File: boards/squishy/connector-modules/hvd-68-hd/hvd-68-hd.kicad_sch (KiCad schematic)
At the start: 14 parts, among them J1 SCSI PHY Mezz, J3 Conn_01x04, J4 HD-68, U1 M24C02-RMC

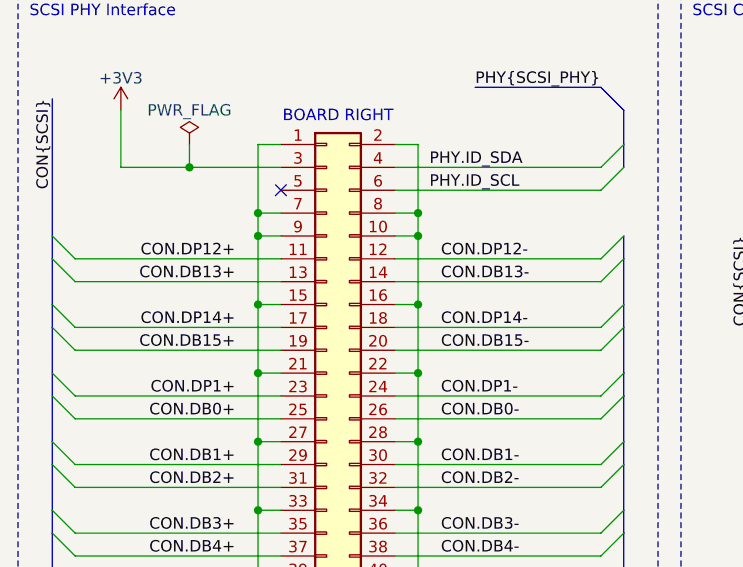
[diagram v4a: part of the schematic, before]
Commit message: squishy: connectors: s/DP12/DB12/g s/DP14/DB14/g
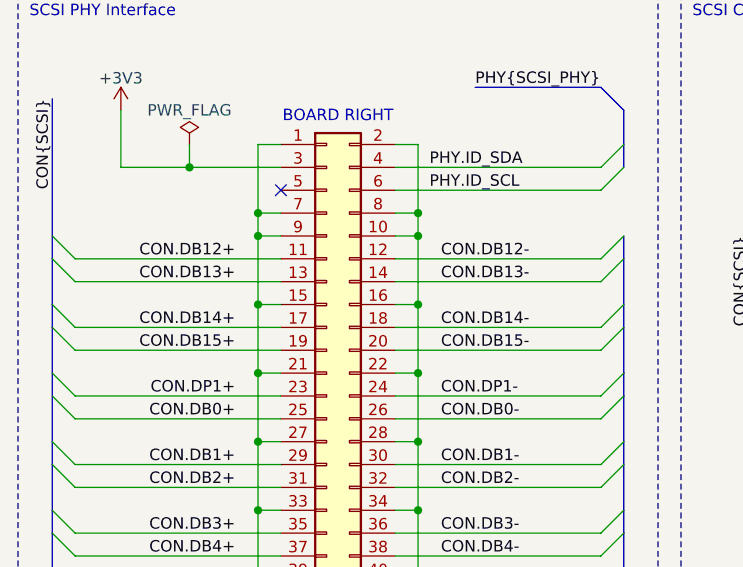
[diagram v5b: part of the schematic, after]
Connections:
- net CON.DP12+ is gone; now on net CON.DB12+: J1.11 (Pin_11)
- net CON.DP12- is gone; now on net CON.DB12-: J1.12 (Pin_12)
- net CON.DP14+ is gone; now on net CON.DB14+: J1.17 (Pin_17)
- net CON.DP14- is gone; now on net CON.DB14-: J1.18 (Pin_18)
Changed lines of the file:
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@@
 		)
 	)
-	(label "CON.DP14-"
+	(label "CON.DB14-"
 		(at 60.96 52.07 0)
 		(fields_autoplaced yes)
@@
 		)
 	)
-	(label "CON.DP12+"
+	(label "CON.DB12+"
 		(at 38.1 44.45 180)
 		(fields_autoplaced yes)
@@
 		)
 	)
-	(label "CON.DP12-"
+	(label "CON.DB12-"
 		(at 60.96 44.45 0)
 		(fields_autoplaced yes)
@@
 		)
 	)
-	(label "CON.DP14+"
+	(label "CON.DB14+"
 		(at 38.1 52.07 180)
 		(fields_autoplaced yes)

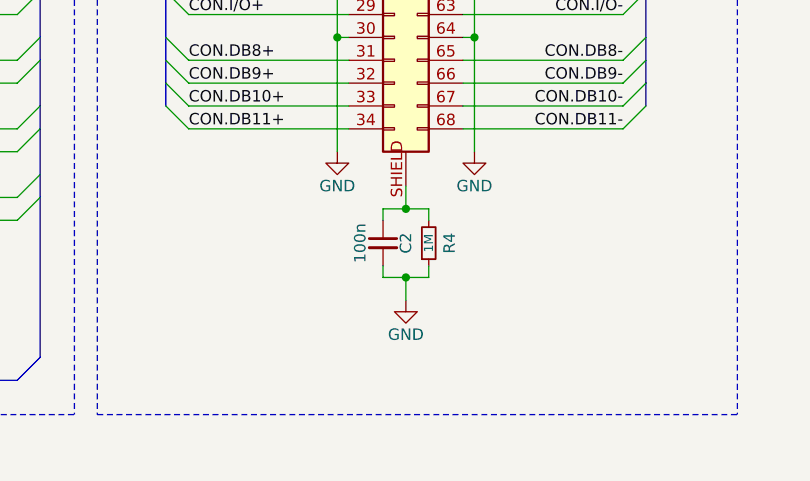
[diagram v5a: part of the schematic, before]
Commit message: squishy: connectors: Begun routing for hvd-68-hd, adjusting connector alignment
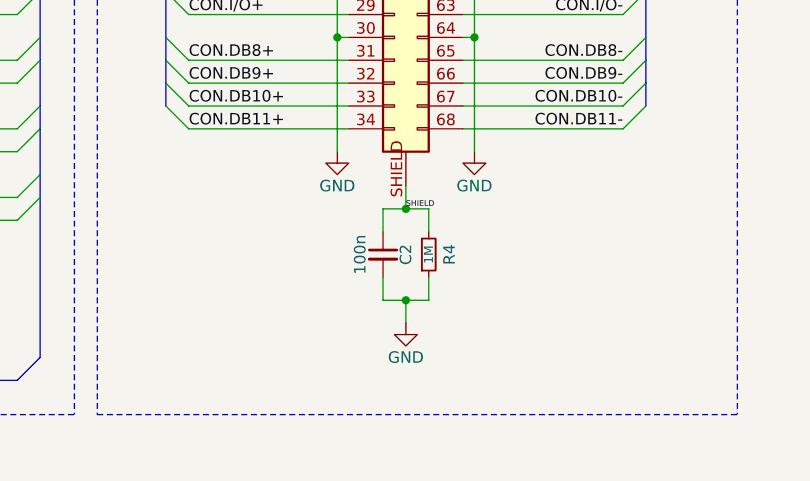
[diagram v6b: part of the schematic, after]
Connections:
- net SHIELD: now reaches C2.1, J4.SHIELD, R4.2
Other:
- moved on the sheet: C2, R4
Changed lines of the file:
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@@
 	)
 	(junction
-		(at 121.92 160.02)
+		(at 121.92 162.56)
 		(diameter 0)
 		(color 0 0 0 0)
@@
 	(wire
 		(pts
-			(xy 124.46 152.4) (xy 124.46 153.67)
+			(xy 124.46 152.4) (xy 124.46 154.94)
 		)
 		(stroke
@@
 	(wire
 		(pts
-			(xy 121.92 160.02) (xy 124.46 160.02)
+			(xy 121.92 162.56) (xy 124.46 162.56)
 		)
 		(stroke
@@
 	(wire
 		(pts
-			(xy 119.38 160.02) (xy 121.92 160.02)
+			(xy 119.38 162.56) (xy 121.92 162.56)
 		)
 		(stroke
@@
 	(wire
 		(pts
-			(xy 121.92 160.02) (xy 121.92 162.56)
+			(xy 121.92 162.56) (xy 121.92 165.1)
 		)
 		(stroke
@@
 	(wire
 		(pts
-			(xy 124.46 158.75) (xy 124.46 160.02)
+			(xy 124.46 160.02) (xy 124.46 162.56)
 		)
 		(stroke
@@
 	(wire
 		(pts
-			(xy 119.38 158.75) (xy 119.38 160.02)
+			(xy 119.38 160.02) (xy 119.38 162.56)
 		)
 		(stroke
@@
 	(wire
 		(pts
-			(xy 119.38 152.4) (xy 119.38 153.67)
+			(xy 119.38 152.4) (xy 119.38 154.94)
 		)
 		(stroke
@@
 		)
 	)
+	(label "SHIELD"
+		(at 121.92 152.4 0)
+		(fields_autoplaced yes)
+		(effects
+			(font
+				(size 0.635 0.635)
+			)
+			(justify left bottom)
+		)
+	)
 	(label "CON.DB13+"
 		(at 38.1 46.99 180)
@@
 	(symbol
 		(lib_id "power:GND")
-		(at 121.92 162.56 0)
+		(at 121.92 165.1 0)
 		(unit 1)
 		(exclude_from_sim no)
@@
 		(dnp no)
 		(property "Reference" "#PWR012"
-			(at 121.92 168.91 0)
+			(at 121.92 171.45 0)
 			(effects
 				(font
@@
 		)
 		(property "Value" "GND"
-			(at 121.92 166.37 0)
+			(at 121.92 168.91 0)
 			(effects
 				(font
@@
 		)
 		(property "Footprint" ""
-			(at 121.92 162.56 0)
+			(at 121.92 165.1 0)
 			(effects
 				(font
@@
 		)
 		(property "Datasheet" ""
-			(at 121.92 162.56 0)
+			(at 121.92 165.1 0)
 			(effects
 				(font
@@
 		)
 		(property "Description" "Power symbol creates a global label with name \"GND\" , ground"
-			(at 121.92 162.56 0)
+			(at 121.92 165.1 0)
 			(effects
 				(font
@@
 	(symbol
 		(lib_id "Device:C_Small")
-		(at 119.38 156.21 0)
+		(at 119.38 157.48 0)
 		(unit 1)
 		(exclude_from_sim no)
@@
 		(dnp no)
 		(property "Reference" "C2"
-			(at 121.92 156.21 90)
+			(at 121.92 157.48 90)
 			(effects
 				(font
@@
 		)
 		(property "Value" "100n"
-			(at 116.84 156.21 90)
+			(at 116.84 157.48 90)
 			(effects
 				(font
@@
 		)
 		(property "Footprint" "rhais_rcl:C0603"
-			(at 119.38 156.21 0)
+			(at 119.38 157.48 0)
 			(effects
 				(font
@@
 		)
 		(property "Datasheet" "https://content.kemet.com/datasheets/KEM_C1006_X5R_SMD.pdf"
-			(at 119.38 156.21 0)
+			(at 119.38 157.48 0)
 			(effects
 				(font
@@
 		)
 		(property "Description" ""
-			(at 119.38 156.21 0)
+			(at 119.38 157.48 0)
 			(effects
 				(font
@@
 		)
 		(property "MFR" "KEMET"
-			(at 119.38 156.21 90)
+			(at 119.38 157.48 90)
 			(effects
 				(font
@@
 		)
 		(property "MPN" "C0603C104M5RACTU"
-			(at 119.38 156.21 90)
+			(at 119.38 157.48 90)
 			(effects
 				(font
@@
 		)
 		(property "Tolerance" "±20% 50V"
-			(at 119.38 156.21 0)
+			(at 119.38 157.48 0)
 			(effects
 				(font
@@
 		)
 		(property "SUPPLIER" "DigiKey"
-			(at 119.38 156.21 0)
+			(at 119.38 157.48 0)
 			(effects
 				(font
@@
 		)
 		(property "SUPPLIER_OC" "399-C0603C104M5RAC7867DKR-ND"
-			(at 119.38 156.21 0)
+			(at 119.38 157.48 0)
 			(effects
 				(font
@@
 		)
 		(property "SUPPLIER_URL" "https://www.digikey.com/short/8nqzrr4b"
-			(at 119.38 156.21 0)
+			(at 119.38 157.48 0)
 			(effects
 				(font
@@
 	(symbol
 		(lib_id "Device:R_Small")
-		(at 124.46 156.21 0)
+		(at 124.46 157.48 0)
 		(mirror x)
 		(unit 1)
@@
 		(dnp no)
 		(property "Reference" "R4"
-			(at 127.508 156.21 90)
+			(at 127.508 157.48 90)
 			(effects
 				(font
@@
 		)
 		(property "Value" "1M"
-			(at 124.46 156.21 90)
+			(at 124.46 157.48 90)
 			(effects
 				(font
@@
 		)
 		(property "Footprint" "rhais_rcl:R0603"
-			(at 124.46 156.21 0)
+			(at 124.46 157.48 0)
 			(effects
 				(font
@@
 		)
 		(property "Datasheet" ""
-			(at 124.46 156.21 0)
+			(at 124.46 157.48 0)
 			(effects
 				(font
@@
 		)
 		(property "Description" ""
-			(at 124.46 156.21 0)
+			(at 124.46 157.48 0)
 			(effects
 				(font
@@
 		)
 		(property "MFR" ""
-			(at 124.46 156.21 90)
+			(at 124.46 157.48 90)
 			(effects
 				(font
@@
 		)
 		(property "MPN" ""
-			(at 124.46 156.21 90)
+			(at 124.46 157.48 90)
 			(effects
 				(font
@@
 		)
 		(property "Tolerance" ""
-			(at 124.46 156.21 0)
+			(at 124.46 157.48 0)
 			(effects
 				(font
@@
 		)
 		(property "SUPPLIER" "DigiKey"
-			(at 124.46 156.21 0)
+			(at 124.46 157.48 0)
 			(effects
 				(font
@@
 		)
 		(property "SUPPLIER_OC" ""
-			(at 124.46 156.21 0)
+			(at 124.46 157.48 0)
 			(effects
 				(font
@@
 		)
 		(property "SUPPLIER_URL" ""
-			(at 124.46 156.21 0)
+			(at 124.46 157.48 0)
 			(effects
 				(font

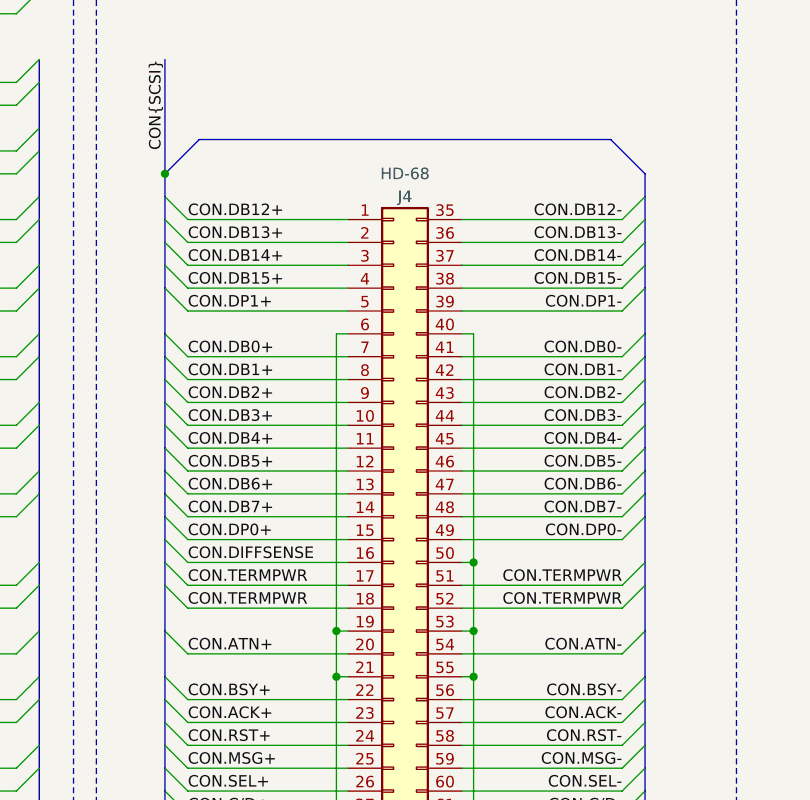
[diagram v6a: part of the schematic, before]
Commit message: squishy: connectors: updated SCSI connector metadata for hvd-68-hd
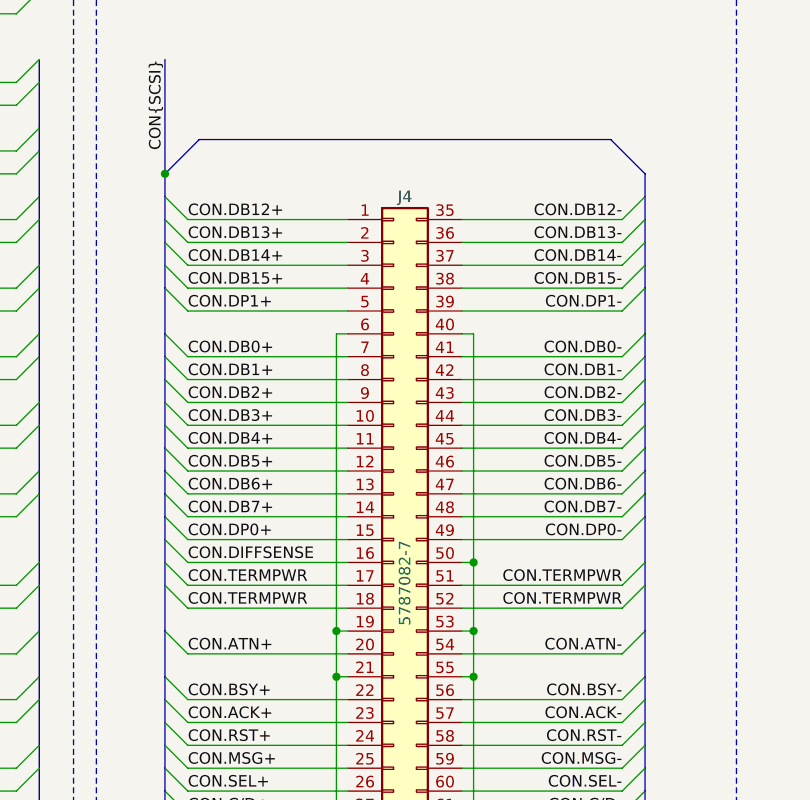
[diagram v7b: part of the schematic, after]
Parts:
- J4: value HD-68 -> 5787082-7; MFR (none) -> TE Connectivity; MPN (none) -> 5787082-7; URL (none) -> https://www.te.com/en/product-5787082-7.html
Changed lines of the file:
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@@
 			)
 		)
-		(property "Value" "HD-68"
-			(at 121.92 54.61 0)
+		(property "Value" "5787082-7"
+			(at 121.92 100.076 90)
 			(effects
 				(font
@@
 			)
 		)
-		(property "Datasheet" "~"
+		(property "Datasheet" "https://www.te.com/commerce/DocumentDelivery/DDEController?Action=showdoc&DocId=Specification+Or+Standard%7F114-40029%7FJ%7Fpdf%7FEnglish%7FENG_SS_114-40029_J.pdf%7F5787082-5"
 			(at 120.65 107.95 0)
 			(effects
@@
 			)
 		)
-		(property "Description" "Generic connector, double row, 02x34 counter clockwise pin numbering scheme (similar to DIP package numbering), with shielding"
+		(property "Description" "AMPLITE 1.27mm High-density D-subminiature 68-pin connector"
 			(at 121.92 100.076 0)
 			(effects
 				(font
+					(size 1.27 1.27)
+				)
+				(hide yes)
+			)
+		)
+		(property "MFR" "TE Connectivity"
+			(at 121.92 100.33 0)
+			(effects
+				(font
+					(size 1.27 1.27)
+				)
+				(hide yes)
+			)
+		)
+		(property "MPN" "5787082-7"
+			(at 121.92 100.33 0)
+			(effects
+				(font
+					(size 1.27 1.27)
+				)
+				(hide yes)
+			)
+		)
+		(property "URL" "https://www.te.com/en/product-5787082-7.html"
+			(at 121.92 100.33 0)
+			(effects
+				(font

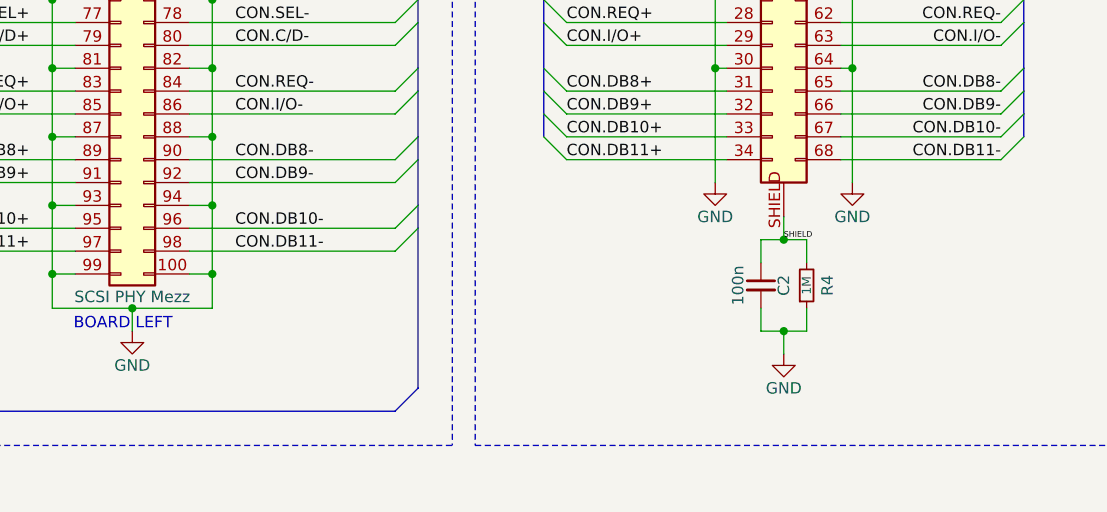
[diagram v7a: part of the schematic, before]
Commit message: squishy: connectors: Adjustments for ERC and DRC cleanliness for hvd-68-hd connector interface board
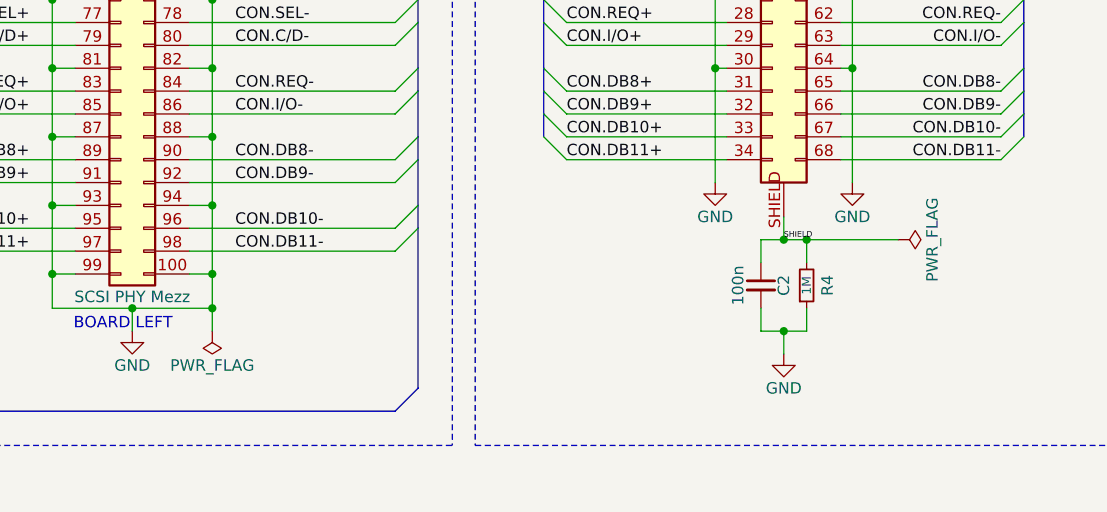
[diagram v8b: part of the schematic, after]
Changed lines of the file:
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@@
 	)
 	(junction
+		(at 124.46 152.4)
+		(diameter 0)
+		(color 0 0 0 0)
+	)
+	(junction
 		(at 58.42 87.63)
 		(diameter 0)
@@
 	)
 	(junction
+		(at 58.42 160.02)
+		(diameter 0)
+		(color 0 0 0 0)
+	)
+	(junction
 		(at 40.64 39.37)
 		(diameter 0)
@@
 	(wire
 		(pts
+			(xy 124.46 152.4) (xy 134.62 152.4)
+		)
+		(stroke
+			(width 0)
+			(type default)
+		)
+	)
+	(wire
+		(pts
 			(xy 265.43 153.67) (xy 264.16 152.4)
 		)
@@
 		)
 	)
+	(wire
+		(pts
+			(xy 58.42 160.02) (xy 58.42 162.56)
+		)
+		(stroke
+			(width 0)
+			(type default)
+		)
+	)
 	(bus
 		(pts
@@
 					(unit 1)
 				)
+			)
+		)
+	)
+	(symbol
+		(lib_id "power:PWR_FLAG")
+		(at 134.62 152.4 270)
+		(unit 1)
+		(exclude_from_sim no)
+		(in_bom yes)
+		(on_board yes)
+		(dnp no)
+		(property "Reference" "#FLG03"
+			(at 136.525 152.4 0)
+			(effects
+				(font
+					(size 1.27 1.27)
+				)
+				(hide yes)
+			)
+		)
+		(property "Value" "PWR_FLAG"
+			(at 138.43 152.4 0)
+			(effects
+				(font
+					(size 1.27 1.27)
+				)
+			)
+		)
+		(property "Footprint" ""
+			(at 134.62 152.4 0)
+			(effects
+				(font
+					(size 1.27 1.27)
+				)
+				(hide yes)
+			)
+		)
+		(property "Datasheet" "~"
+			(at 134.62 152.4 0)
+			(effects
+				(font
+					(size 1.27 1.27)
+				)
+				(hide yes)
+			)
+		)
+		(property "Description" "Special symbol for telling ERC where power comes from"
+			(at 134.62 152.4 0)
+			(effects
+				(font
+					(size 1.27 1.27)
+				)
+				(hide yes)
+			)
+		)
+		(pin "1"
+		)
+		(instances
+			(project "hvd-68-hd"
+				(path "/bd9eafec-5355-49e4-b2e3-916daacb0a86"
+					(reference "#FLG03")
+					(unit 1)
+				)
+			)
+		)
+	)
+	(symbol
+		(lib_id "power:PWR_FLAG")
+		(at 58.42 162.56 180)
+		(unit 1)
+		(exclude_from_sim no)
+		(in_bom yes)
+		(on_board yes)
+		(dnp no)
+		(property "Reference" "#FLG02"
+			(at 58.42 164.465 0)
+			(effects
+				(font
+					(size 1.27 1.27)
+				)
+				(hide yes)
+			)
+		)
+		(property "Value" "PWR_FLAG"
+			(at 58.42 166.37 0)
+			(effects
+				(font
+					(size 1.27 1.27)
+				)
+			)
+		)
+		(property "Footprint" ""
+			(at 58.42 162.56 0)
+			(effects
+				(font
+					(size 1.27 1.27)
+				)
+				(hide yes)
+			)
+		)
+		(property "Datasheet" "~"
+			(at 58.42 162.56 0)
+			(effects
+				(font
+					(size 1.27 1.27)
+				)
+				(hide yes)
+			)
+		)
+		(property "Description" "Special symbol for telling ERC where power comes from"
+			(at 58.42 162.56 0)
+			(effects
+				(font
+					(size 1.27 1.27)
+				)
+				(hide yes)
+			)
+		)
+		(pin "1"
+		)
+		(instances
+			(project "hvd-68-hd"
+				(path "/bd9eafec-5355-49e4-b2e3-916daacb0a86"
+					(reference "#FLG02")
+					(unit 1)
+				)
